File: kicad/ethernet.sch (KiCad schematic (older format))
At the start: 48 parts, among them U2 NUP4114UPXV6T1G, U3 NUP4114UPXV6T1G, X1 L829-1J1T-43

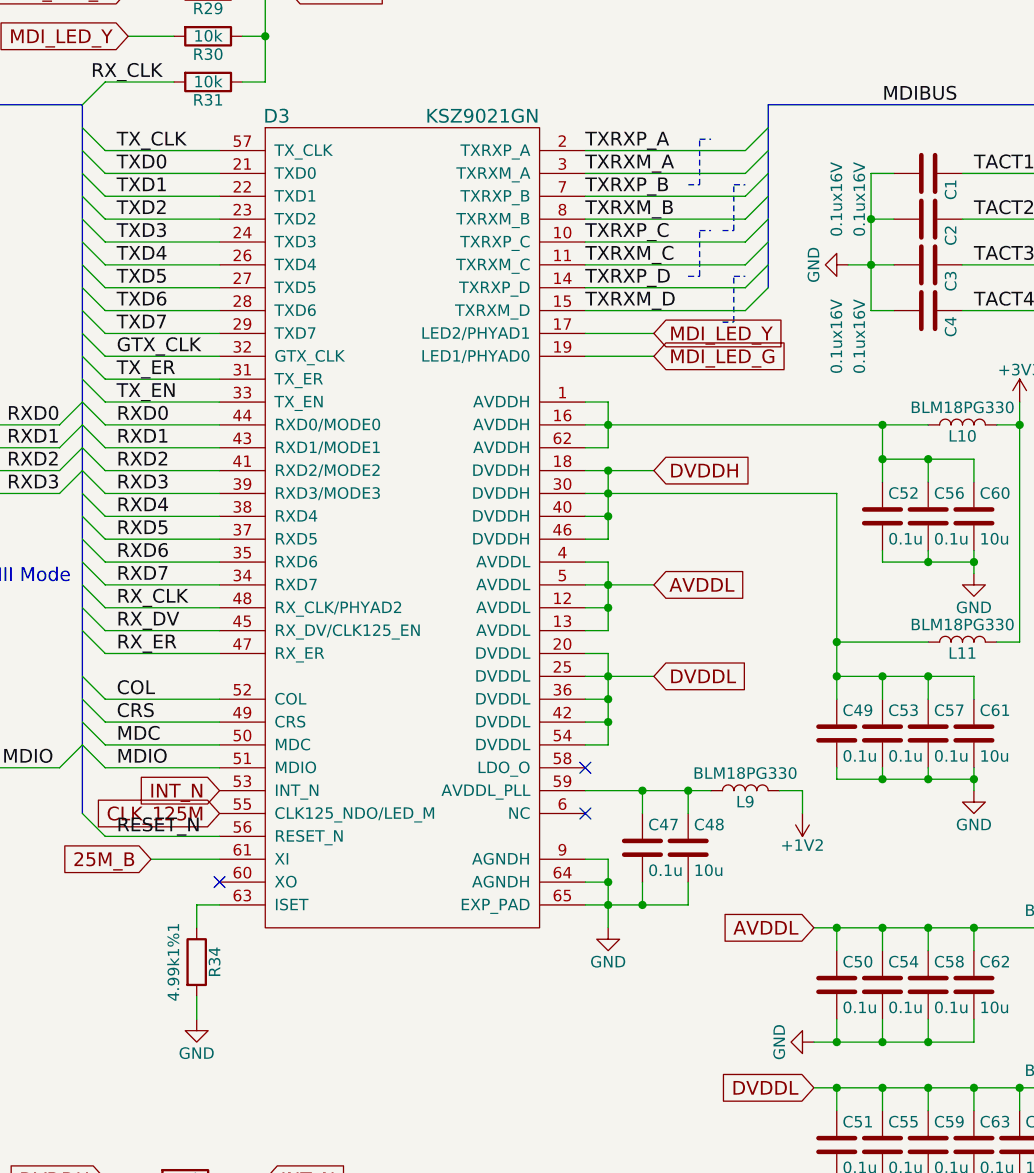
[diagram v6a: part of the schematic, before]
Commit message: place components to pcb, add footprints of cfps-73 l829 sot-563
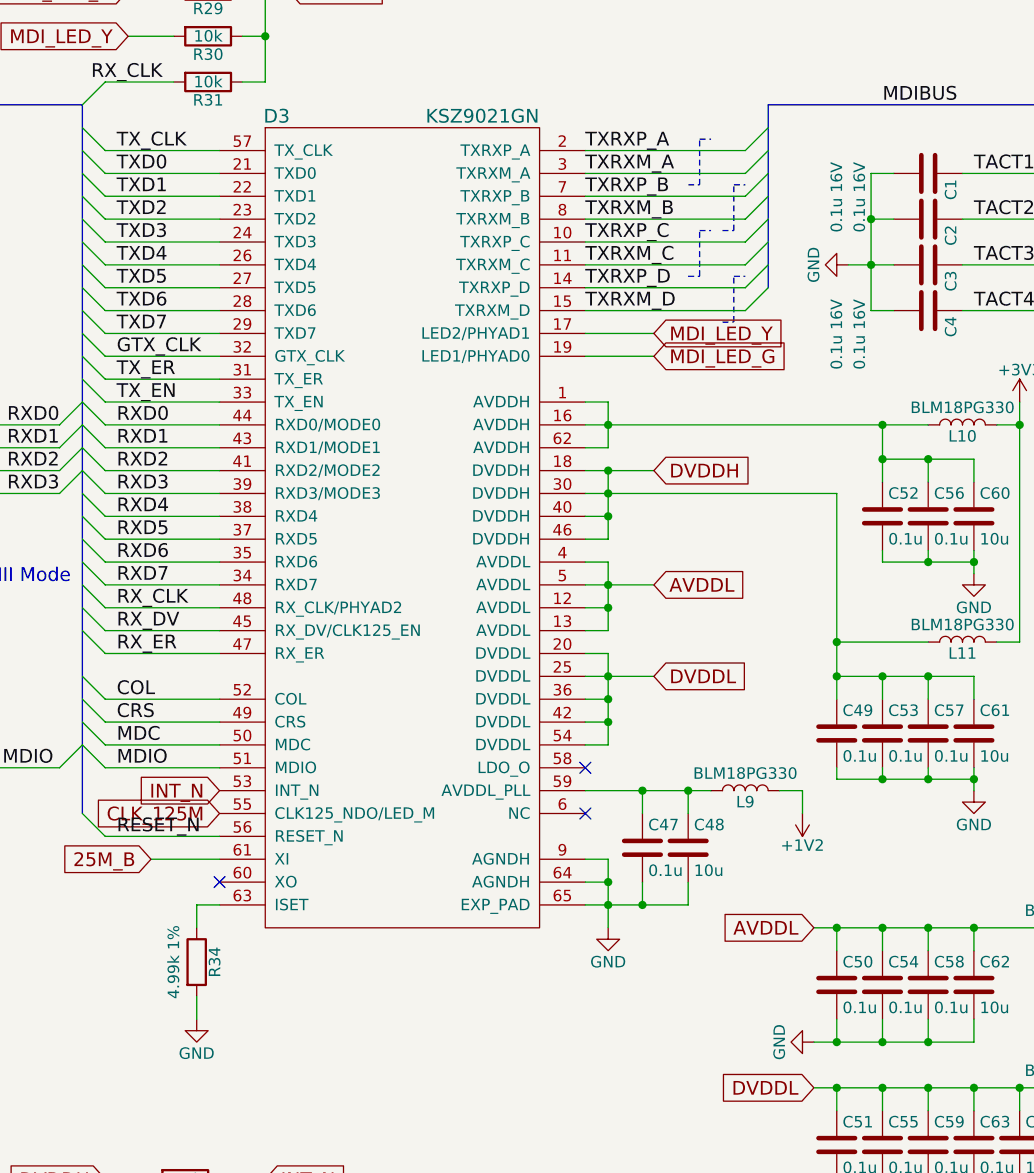
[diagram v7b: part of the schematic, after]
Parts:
- C1, C2, C3, C4: value 0.1ux16V -> 0.1u 16V; footprint (none) -> Capacitors_SMD:C_0603_HandSoldering
- C46, C47, C48, C49, C50, C51, C52, C53, C54, C55, C56, C57, C58, C59, C60, C61, C62, C63, C64: footprint (none) -> Capacitors_SMD:C_0603_HandSoldering
- D3: footprint (none) -> Housings_DFN_QFN:QFN-64-1EP_9x9mm_Pitch0.5mm
- L1, L10, L11, L12, L13, L9: footprint (none) -> Inductors_SMD:L_0603_HandSoldering
- R34: value 4.99k1%1 -> 4.99k 1%; footprint (none) -> Resistors_SMD:R_0603_HandSoldering
- U2, U3: footprint (none) -> library:SOT-563-6
- X1: footprint (none) -> library:L829
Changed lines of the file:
@@
 F 0 "X1" H 9200 3150 60  0000 C CNN
 F 1 "L829-1J1T-43" H 9950 3150 60  0000 C CNN
-F 2 "" H 9700 2600 60  0001 C CNN
+F 2 "library:L829" H 9700 2600 60  0001 C CNN
 F 3 "" H 9700 2600 60  0001 C CNN
 	1    9700 2300
@@
 F 0 "D3" H 4850 4750 60  0000 C CNN
 F 1 "KSZ9021GN" H 5750 4750 60  0000 C CNN
-F 2 "" H 5150 4000 60  0001 C CNN
+F 2 "Housings_DFN_QFN:QFN-64-1EP_9x9mm_Pitch0.5mm" H 5150 4000 60  0001 C CNN
 F 3 "" H 5150 4000 60  0001 C CNN
 	1    5400 3100
@@
 F 0 "L1" V 9950 3400 50  0000 C CNN
 F 1 "BLM18PG330" V 10075 3400 50  0000 C CNN
-F 2 "" H 10000 3400 50  0001 C CNN
+F 2 "Inductors_SMD:L_0603_HandSoldering" H 10000 3400 50  0001 C CNN
 F 3 "" H 10000 3400 50  0001 C CNN
 	1    10000 3400
@@
 P 7700 1700
 F 0 "C1" H 7725 1800 50  0000 L CNN
-F 1 "0.1ux16V" H 7650 1400 50  0000 L CNN
-F 2 "" H 7738 1550 50  0001 C CNN
+F 1 "0.1u 16V" H 7650 1400 50  0000 L CNN
+F 2 "Capacitors_SMD:C_0603_HandSoldering" H 7738 1550 50  0001 C CNN
 F 3 "" H 7700 1700 50  0001 C CNN
 	1    7700 1700
@@
 P 7700 1900
 F 0 "C2" H 7725 2000 50  0000 L CNN
-F 1 "0.1ux16V" H 7450 1500 50  0000 L CNN
-F 2 "" H 7738 1750 50  0001 C CNN
+F 1 "0.1u 16V" H 7450 1500 50  0000 L CNN
+F 2 "Capacitors_SMD:C_0603_HandSoldering" H 7738 1750 50  0001 C CNN
 F 3 "" H 7700 1900 50  0001 C CNN
 	1    7700 1900
@@
 P 7700 2100
 F 0 "C3" H 7725 2200 50  0000 L CNN
-F 1 "0.1ux16V" H 7850 1800 50  0000 L CNN
-F 2 "" H 7738 1950 50  0001 C CNN
+F 1 "0.1u 16V" H 7850 1800 50  0000 L CNN
+F 2 "Capacitors_SMD:C_0603_HandSoldering" H 7738 1950 50  0001 C CNN
 F 3 "" H 7700 2100 50  0001 C CNN
 	1    7700 2100
@@
 P 7700 2300
 F 0 "C4" H 7725 2400 50  0000 L CNN
-F 1 "0.1ux16V" H 7650 1900 50  0000 L CNN
-F 2 "" H 7738 2150 50  0001 C CNN
+F 1 "0.1u 16V" H 7650 1900 50  0000 L CNN
+F 2 "Capacitors_SMD:C_0603_HandSoldering" H 7738 2150 50  0001 C CNN
 F 3 "" H 7700 2300 50  0001 C CNN
 	1    7700 2300
@@
 P 4500 5150
 F 0 "R34" V 4580 5150 50  0000 C CNN
-F 1 "4.99k1%1" V 4400 5150 50  0000 C CNN
-F 2 "" V 4430 5150 50  0001 C CNN
+F 1 "4.99k 1%" V 4400 5150 50  0000 C CNN
+F 2 "Resistors_SMD:R_0603_HandSoldering" V 4430 5150 50  0001 C CNN
 F 3 "" H 4500 5150 50  0001 C CNN
 	1    4500 5150
@@
 F 0 "C46" H 3075 5950 50  0000 L CNN
 F 1 "0.1u" H 3075 5750 50  0000 L CNN
-F 2 "" H 3088 5700 50  0001 C CNN
+F 2 "Capacitors_SMD:C_0603_HandSoldering" H 3088 5700 50  0001 C CNN
 F 3 "" H 3050 5850 50  0001 C CNN
 	1    3050 5850
@@
 F 0 "C53" H 7525 4250 50  0000 L CNN
 F 1 "0.1u" H 7525 4050 50  0000 L CNN
-F 2 "" H 7538 4000 50  0001 C CNN
+F 2 "Capacitors_SMD:C_0603_HandSoldering" H 7538 4000 50  0001 C CNN
 F 3 "" H 7500 4150 50  0001 C CNN
 	1    7500 4150
@@
 F 0 "C57" H 7725 4250 50  0000 L CNN
 F 1 "0.1u" H 7725 4050 50  0000 L CNN
-F 2 "" H 7738 4000 50  0001 C CNN
+F 2 "Capacitors_SMD:C_0603_HandSoldering" H 7738 4000 50  0001 C CNN
 F 3 "" H 7700 4150 50  0001 C CNN
 	1    7700 4150
@@
 F 0 "C61" H 7925 4250 50  0000 L CNN
 F 1 "10u" H 7925 4050 50  0000 L CNN
-F 2 "" H 7938 4000 50  0001 C CNN
+F 2 "Capacitors_SMD:C_0603_HandSoldering" H 7938 4000 50  0001 C CNN
 F 3 "" H 7900 4150 50  0001 C CNN
 	1    7900 4150
@@
 F 0 "C60" H 7925 3300 50  0000 L CNN
 F 1 "10u" H 7925 3100 50  0000 L CNN
-F 2 "" H 7938 3050 50  0001 C CNN
+F 2 "Capacitors_SMD:C_0603_HandSoldering" H 7938 3050 50  0001 C CNN
 F 3 "" H 7900 3200 50  0001 C CNN
 	1    7900 3200
@@
 F 0 "C49" H 7325 4250 50  0000 L CNN
 F 1 "0.1u" H 7325 4050 50  0000 L CNN
-F 2 "" H 7338 4000 50  0001 C CNN
+F 2 "Capacitors_SMD:C_0603_HandSoldering" H 7338 4000 50  0001 C CNN
 F 3 "" H 7300 4150 50  0001 C CNN
 	1    7300 4150
@@
 F 0 "C52" H 7525 3300 50  0000 L CNN
 F 1 "0.1u" H 7525 3100 50  0000 L CNN
-F 2 "" H 7538 3050 50  0001 C CNN
+F 2 "Capacitors_SMD:C_0603_HandSoldering" H 7538 3050 50  0001 C CNN
 F 3 "" H 7500 3200 50  0001 C CNN
 	1    7500 3200
@@
 F 0 "C56" H 7725 3300 50  0000 L CNN
 F 1 "0.1u" H 7725 3100 50  0000 L CNN
-F 2 "" H 7738 3050 50  0001 C CNN
+F 2 "Capacitors_SMD:C_0603_HandSoldering" H 7738 3050 50  0001 C CNN
 F 3 "" H 7700 3200 50  0001 C CNN
 	1    7700 3200
@@
 F 0 "L10" V 7800 2800 50  0000 C CNN
 F 1 "BLM18PG330" V 7925 2800 50  0000 C CNN
-F 2 "" H 7850 2800 50  0001 C CNN
+F 2 "Inductors_SMD:L_0603_HandSoldering" H 7850 2800 50  0001 C CNN
 F 3 "" H 7850 2800 50  0001 C CNN
 	1    7850 2800
@@
 F 0 "L11" V 7800 3750 50  0000 C CNN
 F 1 "BLM18PG330" V 7925 3750 50  0000 C CNN
-F 2 "" H 7850 3750 50  0001 C CNN
+F 2 "Inductors_SMD:L_0603_HandSoldering" H 7850 3750 50  0001 C CNN
 F 3 "" H 7850 3750 50  0001 C CNN
 	1    7850 3750
@@
 F 0 "C48" H 6675 4750 50  0000 L CNN
 F 1 "10u" H 6675 4550 50  0000 L CNN
-F 2 "" H 6688 4500 50  0001 C CNN
+F 2 "Capacitors_SMD:C_0603_HandSoldering" H 6688 4500 50  0001 C CNN
 F 3 "" H 6650 4650 50  0001 C CNN
 	1    6650 4650
@@
 F 0 "C59" H 7725 6050 50  0000 L CNN
 F 1 "0.1u" H 7725 5850 50  0000 L CNN
-F 2 "" H 7738 5800 50  0001 C CNN
+F 2 "Capacitors_SMD:C_0603_HandSoldering" H 7738 5800 50  0001 C CNN
 F 3 "" H 7700 5950 50  0001 C CNN
 	1    7700 5950
@@
 F 0 "C63" H 7925 6050 50  0000 L CNN
 F 1 "0.1u" H 7925 5850 50  0000 L CNN
-F 2 "" H 7938 5800 50  0001 C CNN
+F 2 "Capacitors_SMD:C_0603_HandSoldering" H 7938 5800 50  0001 C CNN
 F 3 "" H 7900 5950 50  0001 C CNN
 	1    7900 5950
@@
 F 0 "C55" H 7525 6050 50  0000 L CNN
 F 1 "0.1u" H 7525 5850 50  0000 L CNN
-F 2 "" H 7538 5800 50  0001 C CNN
+F 2 "Capacitors_SMD:C_0603_HandSoldering" H 7538 5800 50  0001 C CNN
 F 3 "" H 7500 5950 50  0001 C CNN
 	1    7500 5950
@@
 F 0 "C64" H 8125 6050 50  0000 L CNN
 F 1 "10u" H 8125 5850 50  0000 L CNN
-F 2 "" H 8138 5800 50  0001 C CNN
+F 2 "Capacitors_SMD:C_0603_HandSoldering" H 8138 5800 50  0001 C CNN
 F 3 "" H 8100 5950 50  0001 C CNN
 	1    8100 5950
@@
 F 0 "C58" H 7725 5350 50  0000 L CNN
 F 1 "0.1u" H 7725 5150 50  0000 L CNN
-F 2 "" H 7738 5100 50  0001 C CNN
+F 2 "Capacitors_SMD:C_0603_HandSoldering" H 7738 5100 50  0001 C CNN
 F 3 "" H 7700 5250 50  0001 C CNN
 	1    7700 5250
@@
 F 0 "C62" H 7925 5350 50  0000 L CNN
 F 1 "10u" H 7925 5150 50  0000 L CNN
-F 2 "" H 7938 5100 50  0001 C CNN
+F 2 "Capacitors_SMD:C_0603_HandSoldering" H 7938 5100 50  0001 C CNN
 F 3 "" H 7900 5250 50  0001 C CNN
 	1    7900 5250
@@
 F 0 "C50" H 7325 5350 50  0000 L CNN
 F 1 "0.1u" H 7325 5150 50  0000 L CNN
-F 2 "" H 7338 5100 50  0001 C CNN
+F 2 "Capacitors_SMD:C_0603_HandSoldering" H 7338 5100 50  0001 C CNN
 F 3 "" H 7300 5250 50  0001 C CNN
 	1    7300 5250
@@
 F 0 "C54" H 7525 5350 50  0000 L CNN
 F 1 "0.1u" H 7525 5150 50  0000 L CNN
-F 2 "" H 7538 5100 50  0001 C CNN
+F 2 "Capacitors_SMD:C_0603_HandSoldering" H 7538 5100 50  0001 C CNN
 F 3 "" H 7500 5250 50  0001 C CNN
 	1    7500 5250
@@
 F 0 "L9" V 6850 4400 50  0000 C CNN
 F 1 "BLM18PG330" V 6975 4400 50  0000 C CNN
-F 2 "" H 6900 4400 50  0001 C CNN
+F 2 "Inductors_SMD:L_0603_HandSoldering" H 6900 4400 50  0001 C CNN
 F 3 "" H 6900 4400 50  0001 C CNN
 	1    6900 4400
@@
 F 0 "L13" V 8300 5700 50  0000 C CNN
 F 1 "BLM18PG330" V 8425 5700 50  0000 C CNN
-F 2 "" H 8350 5700 50  0001 C CNN
+F 2 "Inductors_SMD:L_0603_HandSoldering" H 8350 5700 50  0001 C CNN
 F 3 "" H 8350 5700 50  0001 C CNN
 	1    8350 5700
@@
 F 0 "L12" V 8300 5000 50  0000 C CNN
 F 1 "BLM18PG330" V 8425 5000 50  0000 C CNN
-F 2 "" H 8350 5000 50  0001 C CNN
+F 2 "Inductors_SMD:L_0603_HandSoldering" H 8350 5000 50  0001 C CNN
 F 3 "" H 8350 5000 50  0001 C CNN
 	1    8350 5000
@@
 F 0 "C47" H 6475 4750 50  0000 L CNN
 F 1 "0.1u" H 6475 4550 50  0000 L CNN
-F 2 "" H 6488 4500 50  0001 C CNN
+F 2 "Capacitors_SMD:C_0603_HandSoldering" H 6488 4500 50  0001 C CNN
 F 3 "" H 6450 4650 50  0001 C CNN
 	1    6450 4650
@@
 F 0 "C51" H 7325 6050 50  0000 L CNN
 F 1 "0.1u" H 7325 5850 50  0000 L CNN
-F 2 "" H 7338 5800 50  0001 C CNN
+F 2 "Capacitors_SMD:C_0603_HandSoldering" H 7338 5800 50  0001 C CNN
 F 3 "" H 7300 5950 50  0001 C CNN
 	1    7300 5950
@@
 F 0 "U2" H 10050 4250 60  0000 C CNN
 F 1 "NUP4114UPXV6T1G" H 10250 3650 60  0000 C CNN
-F 2 "" H 10250 3900 60  0001 C CNN
+F 2 "library:SOT-563-6" H 10250 3900 60  0001 C CNN
 F 3 "" H 10250 3900 60  0001 C CNN
 	1    10250 3950
@@
 F 0 "U3" H 10050 5150 60  0000 C CNN
 F 1 "NUP4114UPXV6T1G" H 10250 4550 60  0000 C CNN
-F 2 "" H 10250 4800 60  0001 C CNN
+F 2 "library:SOT-563-6" H 10250 4800 60  0001 C CNN
 F 3 "" H 10250 4800 60  0001 C CNN
 	1    10250 4850

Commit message: add modeles to 3d render
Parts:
- D2: footprint (none) -> library:EQFP-144_20x20mm_Pitch0.5mm
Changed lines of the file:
@@
 F 0 "D2" H 1200 2750 60  0000 C CNN
 F 1 "10cl025" H 1800 2750 60  0000 C CNN
-F 2 "" H 550 2450 60  0001 C CNN
+F 2 "library:EQFP-144_20x20mm_Pitch0.5mm" H 550 2450 60  0001 C CNN
 F 3 "" H 550 2450 60  0001 C CNN
 	4    1550 2100
@@
 F 0 "D2" H 1200 4250 60  0000 C CNN
 F 1 "10cl025" H 1800 4250 60  0000 C CNN
-F 2 "" H 550 3950 60  0001 C CNN
+F 2 "library:EQFP-144_20x20mm_Pitch0.5mm" H 550 3950 60  0001 C CNN
 F 3 "" H 550 3950 60  0001 C CNN
 	7    1550 3600
@@
 F 0 "D2" H 1200 5650 60  0000 C CNN
 F 1 "10cl025" H 1800 5650 60  0000 C CNN
-F 2 "" H 550 5350 60  0001 C CNN
+F 2 "library:EQFP-144_20x20mm_Pitch0.5mm" H 550 5350 60  0001 C CNN
 F 3 "" H 550 5350 60  0001 C CNN
 	8    1550 5000
